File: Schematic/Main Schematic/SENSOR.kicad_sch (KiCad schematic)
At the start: 11 parts, among them IC2 LM75AD,118

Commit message: Update
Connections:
- net +3V3 renamed 3.3V
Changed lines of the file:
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@@
   (junction (at 110.6932 125.4506) (diameter 0) (color 0 0 0 0)
   )
-  (junction (at 113.1824 100.0506) (diameter 0) (color 0 0 0 0)
+  (junction (at 113.2332 100.0506) (diameter 0) (color 0 0 0 0)
   )
   (junction (at 113.2332 105.7656) (diameter 0) (color 0 0 0 0)
@@
     (stroke (width 0) (type default))
   )
+  (wire (pts (xy 113.2332 92.4052) (xy 113.1824 92.4052))
+    (stroke (width 0) (type default))
+  )
   (wire (pts (xy 180.4416 111.379) (xy 180.4416 112.649))
     (stroke (width 0) (type default))
@@
     (stroke (width 0) (type default))
   )
-  (wire (pts (xy 110.6932 100.0506) (xy 113.1824 100.0506))
-    (stroke (width 0) (type default))
-  )
   (wire (pts (xy 85.2932 127.9906) (xy 85.2932 132.4356))
     (stroke (width 0) (type default))
@@
     (stroke (width 0) (type default))
   )
+  (wire (pts (xy 113.2332 92.4052) (xy 113.2332 100.0506))
+    (stroke (width 0) (type default))
+  )
+  (wire (pts (xy 70.0532 105.7656) (xy 78.9432 105.7656))
+    (stroke (width 0) (type default))
+  )
+  (polyline (pts (xy 155.956 143.2306) (xy 214.884 143.0782))
+    (stroke (width 0) (type default))
+  )
+  (polyline (pts (xy 156.0068 84.6582) (xy 156.1592 143.5862))
+    (stroke (width 0) (type default))
+  )
+  (wire (pts (xy 110.6932 125.4506) (xy 110.6932 127.9906))
+    (stroke (width 0) (type default))
+  )
+  (wire (pts (xy 70.0532 122.9106) (xy 70.0532 113.3856))
+    (stroke (width 0) (type default))
+  )
+  (polyline (pts (xy 121.4628 83.185) (xy 57.2516 83.5914))
+    (stroke (width 0) (type default))
+  )
+  (wire (pts (xy 85.2932 120.3706) (xy 82.1182 120.3706))
+    (stroke (width 0) (type default))
+  )
+  (wire (pts (xy 97.9932 100.0506) (xy 87.8332 100.0506))
+    (stroke (width 0) (type default))
+  )
+  (wire (pts (xy 164.1856 107.7214) (xy 164.1856 111.379))
+    (stroke (width 0) (type default))
+  )
+  (polyline (pts (xy 214.4776 84.4042) (xy 214.63 143.3322))
+    (stroke (width 0) (type default))
+  )
+  (wire (pts (xy 62.4332 105.7656) (xy 70.0532 105.7656))
+    (stroke (width 0) (type default))
+  )
+  (wire (pts (xy 110.6932 122.9106) (xy 110.6932 125.4506))
+    (stroke (width 0) (type default))
+  )
+  (wire (pts (xy 65.6082 125.4506) (xy 85.2932 125.4506))
+    (stroke (width 0) (type default))
+  )
+  (wire (pts (xy 180.4416 111.379) (xy 202.2856 111.379))
+    (stroke (width 0) (type default))
+  )
   (wire (pts (xy 113.2332 100.0506) (xy 113.2332 105.7656))
     (stroke (width 0) (type default))
   )
-  (wire (pts (xy 70.0532 105.7656) (xy 78.9432 105.7656))
-    (stroke (width 0) (type default))
-  )
-  (polyline (pts (xy 155.956 143.2306) (xy 214.884 143.0782))
-    (stroke (width 0) (type default))
-  )
-  (polyline (pts (xy 156.0068 84.6582) (xy 156.1592 143.5862))
-    (stroke (width 0) (type default))
-  )
-  (wire (pts (xy 110.6932 125.4506) (xy 110.6932 127.9906))
-    (stroke (width 0) (type default))
-  )
-  (wire (pts (xy 70.0532 122.9106) (xy 70.0532 113.3856))
-    (stroke (width 0) (type default))
-  )
-  (polyline (pts (xy 121.4628 83.185) (xy 57.2516 83.5914))
-    (stroke (width 0) (type default))
-  )
-  (wire (pts (xy 113.1824 92.4306) (xy 113.1824 100.0506))
-    (stroke (width 0) (type default))
-  )
-  (wire (pts (xy 85.2932 120.3706) (xy 82.1182 120.3706))
-    (stroke (width 0) (type default))
-  )
-  (wire (pts (xy 97.9932 100.0506) (xy 87.8332 100.0506))
-    (stroke (width 0) (type default))
-  )
-  (wire (pts (xy 164.1856 107.7214) (xy 164.1856 111.379))
-    (stroke (width 0) (type default))
-  )
-  (polyline (pts (xy 214.4776 84.4042) (xy 214.63 143.3322))
-    (stroke (width 0) (type default))
-  )
-  (wire (pts (xy 62.4332 105.7656) (xy 70.0532 105.7656))
-    (stroke (width 0) (type default))
-  )
-  (wire (pts (xy 110.6932 122.9106) (xy 110.6932 125.4506))
-    (stroke (width 0) (type default))
-  )
-  (wire (pts (xy 65.6082 125.4506) (xy 85.2932 125.4506))
-    (stroke (width 0) (type default))
-  )
-  (wire (pts (xy 180.4416 111.379) (xy 202.2856 111.379))
-    (stroke (width 0) (type default))
-  )
   (wire (pts (xy 85.2932 122.9106) (xy 71.9582 122.9106))
     (stroke (width 0) (type default))
@@
     (stroke (width 0) (type default))
   )
-  (wire (pts (xy 113.1824 100.0506) (xy 113.2332 100.0506))
+  (wire (pts (xy 110.6932 100.0506) (xy 113.2332 100.0506))
     (stroke (width 0) (type default))
   )
@@
     (effects (font (size 1.27 1.27)) (justify left bottom))
   )
+  (hierarchical_label "3.3V" (shape input) (at 164.1856 97.1804 0) (fields_autoplaced)
+    (effects (font (size 1.27 1.27)) (justify left))
+  )
   (hierarchical_label "LDR" (shape input) (at 202.2856 111.379 0) (fields_autoplaced)
     (effects (font (size 1.27 1.27)) (justify left))
@@
   (hierarchical_label "SCL" (shape input) (at 70.0532 117.221 180) (fields_autoplaced)
     (effects (font (size 1.27 1.27)) (justify right))
+  )
+  (hierarchical_label "3.3V" (shape input) (at 113.1824 92.4052 0) (fields_autoplaced)
+    (effects (font (size 1.27 1.27)) (justify left))
   )
   (symbol (lib_id "power:GND") (at 110.6932 129.2606 0) (unit 1)
@@
     )
   )
-  (symbol (lib_id "power:+3V3") (at 113.1824 92.4306 0) (unit 1)
-    (in_bom yes) (on_board yes) (dnp no) (fields_autoplaced)
-    (property "Reference" "#PWR016" (at 113.1824 96.2406 0)
-      (effects (font (size 1.27 1.27)) hide)
-    )
-    (property "Value" "+3V3" (at 113.1824 89.1794 0)
-      (effects (font (size 1.27 1.27)))
-    )
-    (property "Footprint" "" (at 113.1824 92.4306 0)
-      (effects (font (size 1.27 1.27)) hide)
-    )
-    (property "Datasheet" "" (at 113.1824 92.4306 0)
-      (effects (font (size 1.27 1.27)) hide)
-    )
-    (pin "1")
-    (instances
-      (project "Main Schematic"
-        (path "/81c41bad-bb43-41af-b405-18d135a809b1/820a1ce6-42c1-4792-8ad0-5e2a5c074ed4"
-          (reference "#PWR016") (unit 1)
-        )
-      )
-    )
-  )
   (symbol (lib_id "Device:R") (at 70.0532 109.5756 0) (unit 1)
     (in_bom yes) (on_board yes) (dnp no) (fields_autoplaced)
@@
         )
       )
-    )
-  )
-  (symbol (lib_id "power:+3V3") (at 164.1856 97.1804 0) (unit 1)
-    (in_bom yes) (on_board yes) (dnp no) (fields_autoplaced)
-    (property "Reference" "#PWR017" (at 164.1856 100.9904 0)
-      (effects (font (size 1.27 1.27)) hide)
-    )
-    (property "Value" "+3V3" (at 164.1856 93.9292 0)
-      (effects (font (size 1.27 1.27)))
-    )
-    (property "Footprint" "" (at 164.1856 97.1804 0)
-      (effects (font (size 1.27 1.27)) hide)
-    )
-    (property "Datasheet" "" (at 164.1856 97.1804 0)
-      (effects (font (size 1.27 1.27)) hide)
-    )
-    (pin "1")
-    (instances
-      (project "Main Schematic"
-        (path "/81c41bad-bb43-41af-b405-18d135a809b1/820a1ce6-42c1-4792-8ad0-5e2a5c074ed4"
-          (reference "#PWR017") (unit 1)
-        )
-      )

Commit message: assigned footprints for most of the components
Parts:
- R?: footprint (none) -> R5K:RESC2012X60N
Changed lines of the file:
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@@
       (effects (font (size 1.27 1.27)) (justify left))
     )
-    (property "Footprint" "" (at 162.4076 103.9114 90)
+    (property "Footprint" "R5K:RESC2012X60N" (at 162.4076 103.9114 90)
       (effects (font (size 1.27 1.27)) hide)
     )

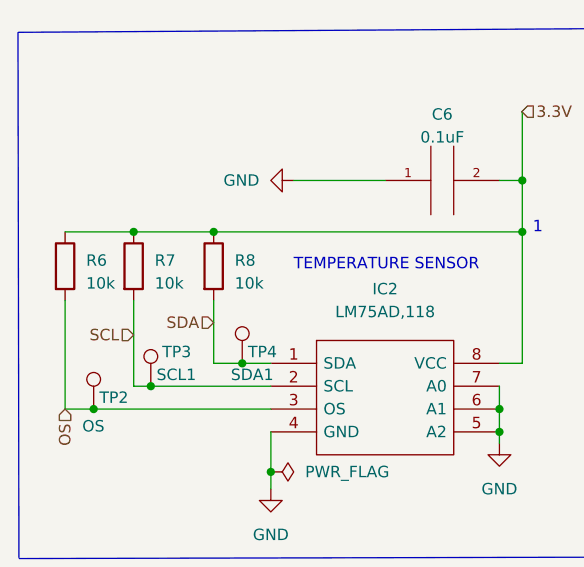
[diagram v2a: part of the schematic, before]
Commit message: Changed sensor resistors
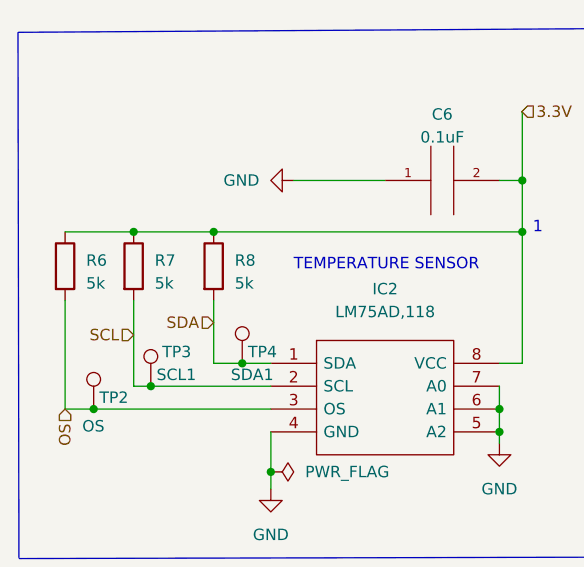
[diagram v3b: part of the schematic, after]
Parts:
- R6, R7, R8: value 10k -> 5k
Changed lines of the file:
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@@
       (effects (font (size 1.27 1.27)) (justify left))
     )
-    (property "Value" "10k" (at 81.28 111.4806 0)
+    (property "Value" "5k" (at 81.28 111.4806 0)
       (effects (font (size 1.27 1.27)) (justify left))
     )
@@
       (effects (font (size 1.27 1.27)) (justify left))
     )
-    (property "Value" "10k" (at 72.39 111.4806 0)
+    (property "Value" "5k" (at 72.39 111.4806 0)
       (effects (font (size 1.27 1.27)) (justify left))
     )
@@
       (effects (font (size 1.27 1.27)) (justify left))
     )
-    (property "Value" "10k" (at 64.77 111.4806 0)
-      (effects (font (size 1.27 1.27)) (justify left))
-    )
+    (property "Value" "5k" (at 64.77 111.4806 0)
+      (effects (font (size 1.27 1.27)) (justify left))
+    )

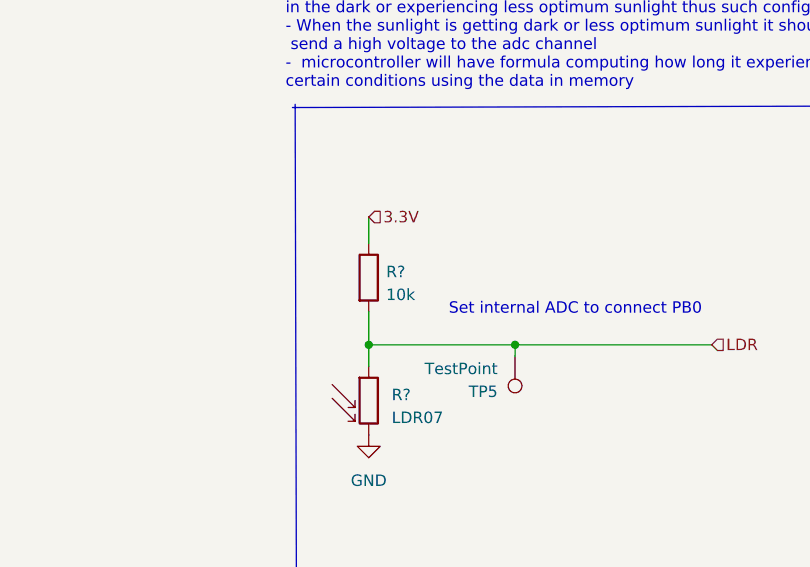
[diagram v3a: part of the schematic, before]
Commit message: Updated sensing R
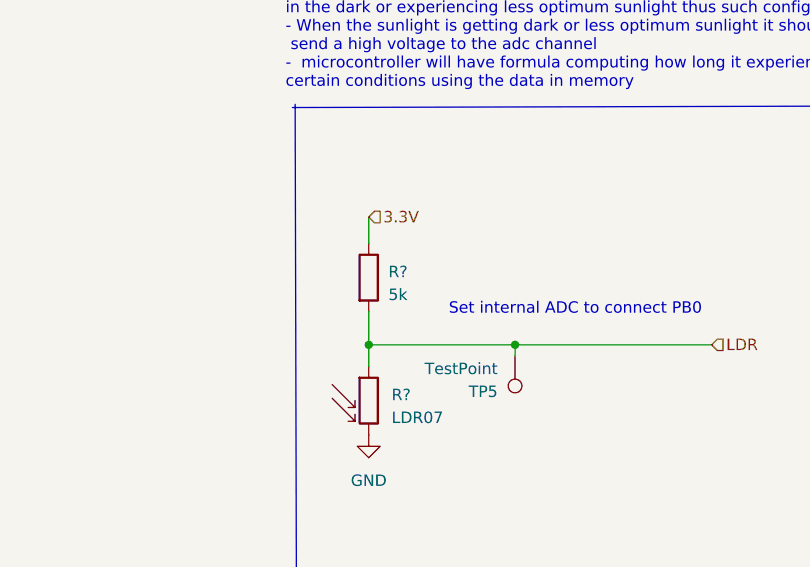
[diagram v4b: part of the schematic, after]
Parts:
- R?: value 10k -> 5k
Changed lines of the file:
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@@
   (symbol (lib_id "Device:R") (at 164.1856 103.9114 0) (unit 1)
     (in_bom yes) (on_board yes) (dnp no) (fields_autoplaced)
-    (property "Reference" "R?" (at 166.116 103.2764 0)
+    (property "Reference" "R?" (at 166.37 103.2764 0)
       (effects (font (size 1.27 1.27)) (justify left))
     )
-    (property "Value" "10k" (at 166.116 105.8164 0)
+    (property "Value" "5k" (at 166.37 105.8164 0)
       (effects (font (size 1.27 1.27)) (justify left))
     )

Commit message: Update
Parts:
- R6, R7, R8, R?: value 5k -> 10k
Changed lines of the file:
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@@
       (effects (font (size 1.27 1.27)) (justify left))
     )
-    (property "Value" "5k" (at 81.28 111.4806 0)
+    (property "Value" "10k" (at 81.28 111.4806 0)
       (effects (font (size 1.27 1.27)) (justify left))
     )
@@
       (effects (font (size 1.27 1.27)) (justify left))
     )
-    (property "Value" "5k" (at 72.39 111.4806 0)
+    (property "Value" "10k" (at 72.39 111.4806 0)
       (effects (font (size 1.27 1.27)) (justify left))
     )
@@
       (effects (font (size 1.27 1.27)) (justify left))
     )
-    (property "Value" "5k" (at 166.37 105.8164 0)
+    (property "Value" "10k" (at 166.37 105.8164 0)
       (effects (font (size 1.27 1.27)) (justify left))
     )
@@
       (effects (font (size 1.27 1.27)) (justify left))
     )
-    (property "Value" "5k" (at 64.77 111.4806 0)
-      (effects (font (size 1.27 1.27)) (justify left))
-    )
+    (property "Value" "10k" (at 64.77 111.4806 0)
+      (effects (font (size 1.27 1.27)) (justify left))
+    )

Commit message: Updated the footprints and the PCB
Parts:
- R6, R7, R8, R?: footprint R5K:RESC2012X60N -> Resistor_SMD:R_1206_3216Metric
- TP5: footprint (none) -> TestPoint:TestPoint_Pad_1.0x1.0mm
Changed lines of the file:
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@@
       (effects (font (size 1.27 1.27)) (justify left))
     )
-    (property "Footprint" "R5K:RESC2012X60N" (at 77.1652 109.5756 90)
+    (property "Footprint" "Resistor_SMD:R_1206_3216Metric" (at 77.1652 109.5756 90)
       (effects (font (size 1.27 1.27)) hide)
     )
@@
       (effects (font (size 1.27 1.27)) (justify left))
     )
-    (property "Footprint" "R5K:RESC2012X60N" (at 68.2752 109.5756 90)
+    (property "Footprint" "Resistor_SMD:R_1206_3216Metric" (at 68.2752 109.5756 90)
       (effects (font (size 1.27 1.27)) hide)
     )
@@
       (effects (font (size 1.27 1.27)) (justify left))
     )
-    (property "Footprint" "R5K:RESC2012X60N" (at 162.4076 103.9114 90)
+    (property "Footprint" "Resistor_SMD:R_1206_3216Metric" (at 162.4076 103.9114 90)
       (effects (font (size 1.27 1.27)) hide)
     )
@@
       (effects (font (size 1.27 1.27)) (justify left))
     )
-    (property "Footprint" "" (at 175.3616 112.649 0)
+    (property "Footprint" "TestPoint:TestPoint_Pad_1.0x1.0mm" (at 175.3616 112.649 0)
       (effects (font (size 1.27 1.27)) hide)
     )
@@
       (effects (font (size 1.27 1.27)) (justify left))
     )
-    (property "Footprint" "R5K:RESC2012X60N" (at 60.6552 109.5756 90)
-      (effects (font (size 1.27 1.27)) hide)
-    )
+    (property "Footprint" "Resistor_SMD:R_1206_3216Metric" (at 60.6552 109.5756 90)
+      (effects (font (size 1.27 1.27)) hide)
+    )
